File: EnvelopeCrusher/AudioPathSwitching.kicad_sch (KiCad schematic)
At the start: 3 parts

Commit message: updated
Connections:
- net SW_SIGNAL renamed RELAY_SIGNAL
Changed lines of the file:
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@@
     (effects (font (size 1.27 1.27)) (justify right))
   )
-  (hierarchical_label "SW_SIGNAL" (shape input) (at 55.88 71.12 180)
+  (hierarchical_label "RELAY_SIGNAL" (shape input) (at 55.88 71.12 180)
     (effects (font (size 1.27 1.27)) (justify right))
   )

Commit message: Completed Schematic
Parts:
- gave numbers to parts that had none: 2
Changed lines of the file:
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@@
   (symbol (lib_id "Device:Q_NMOS_GSD") (at 167.64 71.12 0) (unit 1)
     (in_bom yes) (on_board yes) (fields_autoplaced)
-    (property "Reference" "Q?" (id 0) (at 173.99 69.8499 0)
+    (property "Reference" "Q1" (id 0) (at 173.99 69.8499 0)
       (effects (font (size 1.27 1.27)) (justify left))
     )
@@
   (symbol (lib_id "Device:D") (at 170.18 107.95 270) (unit 1)
     (in_bom yes) (on_board yes) (fields_autoplaced)
-    (property "Reference" "D?" (id 0) (at 172.72 106.6799 90)
+    (property "Reference" "D2" (id 0) (at 172.72 106.6799 90)
       (effects (font (size 1.27 1.27)) (justify left))
     )
@@
   (symbol (lib_id "power:+3.3V") (at 170.18 60.96 0) (unit 1)
     (in_bom yes) (on_board yes) (fields_autoplaced)
-    (property "Reference" "#PWR?" (id 0) (at 170.18 64.77 0)
+    (property "Reference" "#PWR043" (id 0) (at 170.18 64.77 0)
       (effects (font (size 1.27 1.27)) hide)
     )

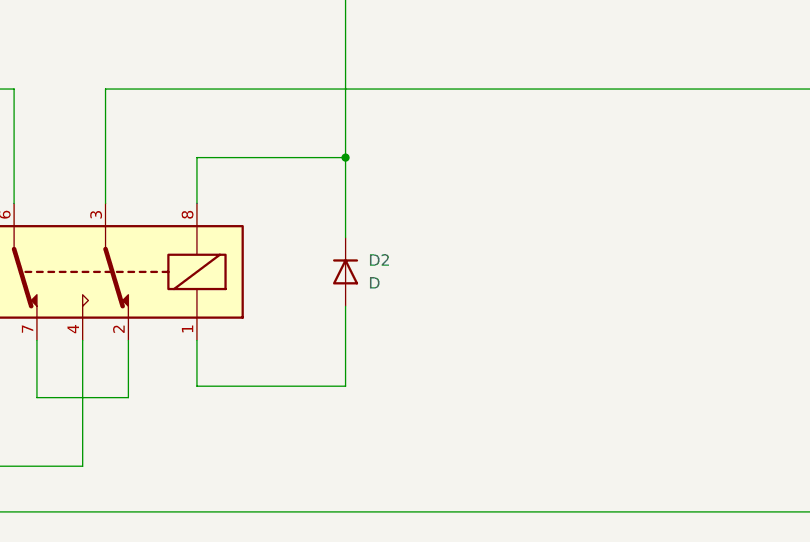
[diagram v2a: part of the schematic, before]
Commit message: updated schematic
- Added values and comments to state-variable filter block
- Updated footprints
- Changed Dual Op Amp: TL072 to AM358
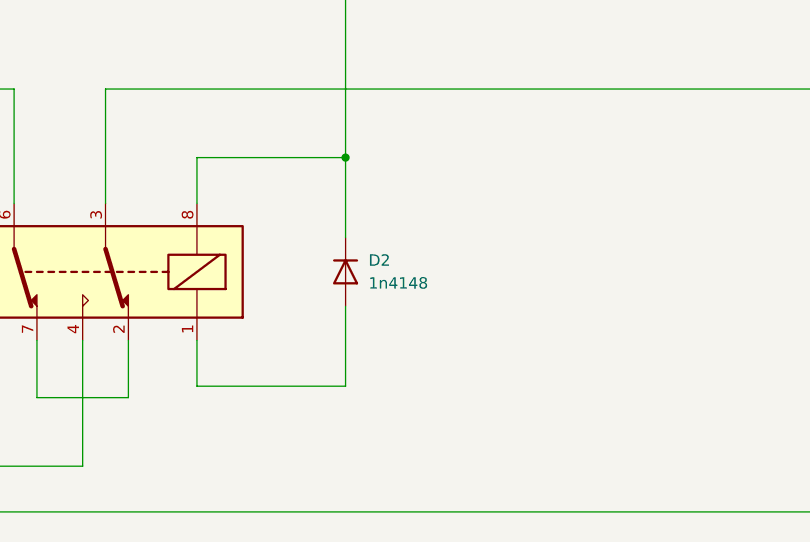
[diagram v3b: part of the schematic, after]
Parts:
- D2: value D -> 1n4148; footprint (none) -> Diode_SMD:D_SOD-123F
- Q1: footprint (none) -> Package_TO_SOT_SMD:SOT-23
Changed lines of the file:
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@@
       (effects (font (size 1.27 1.27)) (justify left))
     )
-    (property "Footprint" "" (id 2) (at 172.72 68.58 0)
+    (property "Footprint" "Package_TO_SOT_SMD:SOT-23" (id 2) (at 172.72 68.58 0)
       (effects (font (size 1.27 1.27)) hide)
     )
-    (property "Datasheet" "~" (id 3) (at 167.64 71.12 0)
+    (property "Datasheet" "https://www.mouser.co.uk/datasheet/2/115/DMG2302U-1512446.pdf" (id 3) (at 167.64 71.12 0)
       (effects (font (size 1.27 1.27)) hide)
     )
@@
       (effects (font (size 1.27 1.27)) (justify left) hide)
     )
-    (property "Datasheet" "" (id 3) (at 143.51 107.95 0)
+    (property "Datasheet" "https://docs.rs-online.com/9c6f/0900766b81587c84.pdf" (id 3) (at 143.51 107.95 0)
       (effects (font (size 1.27 1.27)) hide)
     )
@@
       (effects (font (size 1.27 1.27)) (justify left))
     )
-    (property "Value" "D" (id 1) (at 172.72 109.2199 90)
+    (property "Value" "1n4148" (id 1) (at 172.72 109.2199 90)
       (effects (font (size 1.27 1.27)) (justify left))
     )
-    (property "Footprint" "" (id 2) (at 170.18 107.95 0)
+    (property "Footprint" "Diode_SMD:D_SOD-123F" (id 2) (at 170.18 107.95 0)
       (effects (font (size 1.27 1.27)) hide)
     )

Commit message: organised layout into functional blocks
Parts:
- RL1: footprint Relay_THT:Relay_DPDT_Omron_G2RL -> Relay_SMD:Relay_Fujitsu_FTR-B3S
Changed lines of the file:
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@@
       (effects (font (size 1.27 1.27)) (justify right))
     )
-    (property "Footprint" "Relay_THT:Relay_DPDT_Omron_G2RL" (id 2) (at 127 106.68 0)
+    (property "Footprint" "Relay_SMD:Relay_Fujitsu_FTR-B3S" (id 2) (at 127 106.68 0)
       (effects (font (size 1.27 1.27)) (justify left) hide)
     )
@@
   (symbol (lib_id "power:+3.3V") (at 170.18 60.96 0) (unit 1)
     (in_bom yes) (on_board yes) (fields_autoplaced)
-    (property "Reference" "#PWR043" (id 0) (at 170.18 64.77 0)
+    (property "Reference" "#PWR041" (id 0) (at 170.18 64.77 0)
       (effects (font (size 1.27 1.27)) hide)
     )
